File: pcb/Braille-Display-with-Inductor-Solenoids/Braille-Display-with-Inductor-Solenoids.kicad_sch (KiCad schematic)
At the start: 11 parts, among them J1 Screw_Terminal_01x02, J2 Screw_Terminal_01x02, J3 Screw_Terminal_01x02, U1 RP2040-Zero

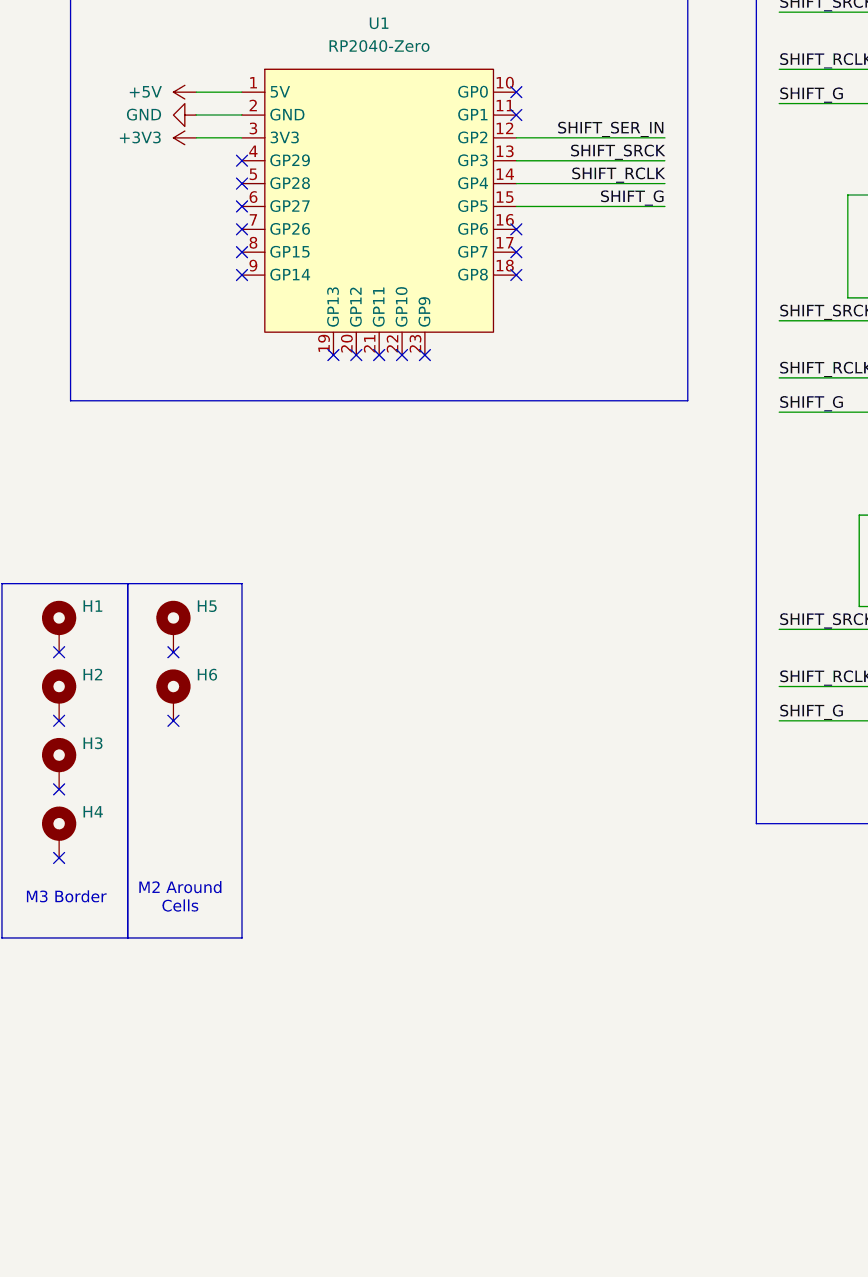
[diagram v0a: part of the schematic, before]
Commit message: Update net class rules for routing
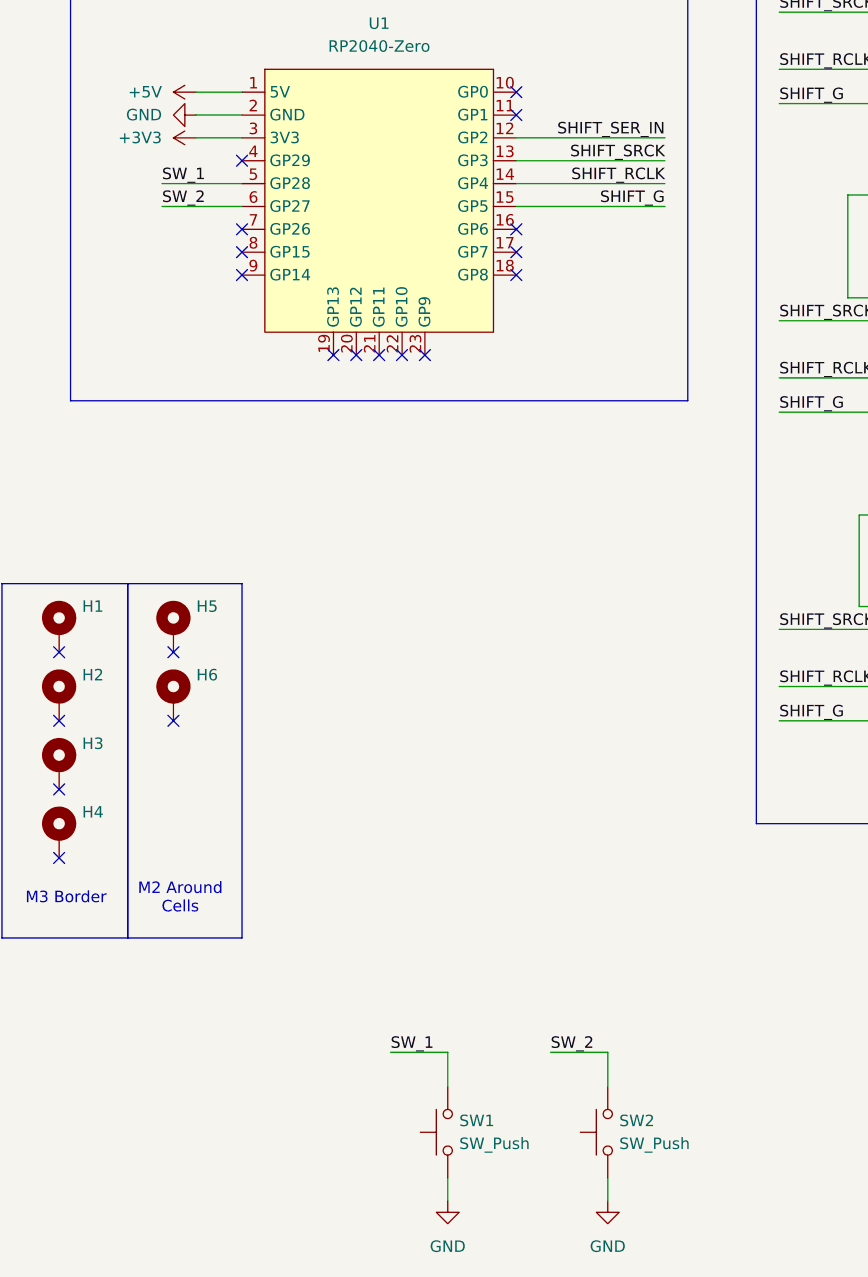
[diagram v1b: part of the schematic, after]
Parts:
- added SW1, SW2: SW_Push, 00-project-footprint-lib:PushButtonSMD_2.93x3.9, symbol Switch:SW_Push
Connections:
- net GND: now also SW1.1, SW2.1
- net SW_1: now reaches U1.5 (GP28)
- net SW_1: now also SW1.2
- net SW_2: now reaches U1.6 (GP27)
- net SW_2: now also SW2.2
- no-connect marks 23 -> 21
